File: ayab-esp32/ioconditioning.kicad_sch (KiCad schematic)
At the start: 45 parts, among them J701 CTRL_3v3, J702 CTRL_5V, U701 SN74LVC4245, U702 LM393, U703 LM393

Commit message: Bypass KH910 K-L comparators and add pull-ups
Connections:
- net EOL_R_K: no longer names the net of J702.6 (Pin_6), R711.1, R712.2, R717.1, U701.8 (A6), U703.1
- net EOL_R_L: no longer names the net of J702.7 (Pin_7), R713.1, R714.2, R718.2, U701.9 (A7), U703.7
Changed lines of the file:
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@@
   (wire (pts (xy 102.87 80.01) (xy 102.87 86.36))
     (stroke (width 0) (type default))
-  )
-  (wire (pts (xy 179.07 144.78) (xy 182.88 144.78))
+  )  (wire (pts (xy 107.95 88.9) (xy 107.95 106.68))
     (stroke (width 0) (type default))
-  )
-  (wire (pts (xy 107.95 88.9) (xy 107.95 106.68))
-    (stroke (width 0) (type default))
-  )
-  (wire (pts (xy 182.88 120.65) (xy 181.61 120.65))
-    (stroke (width 0) (type default))
-  )
-  (wire (pts (xy 170.18 99.06) (xy 181.61 99.06))
+  )  (wire (pts (xy 170.18 99.06) (xy 181.61 99.06))
     (stroke (width 0) (type default))
   )
@@
     (effects (font (size 1.27 1.27)) (justify right))
   )
-  (hierarchical_label "EOL_R_L" (shape input) (at 182.88 144.78 0) (fields_autoplaced)
+    (hierarchical_label "EOL_R_N" (shape output) (at 34.29 101.6 180) (fields_autoplaced)
+    (effects (font (size 1.27 1.27)) (justify right))
+  )
+    (hierarchical_label "EOL_R" (shape input) (at 266.7 114.3 0) (fields_autoplaced)
     (effects (font (size 1.27 1.27)) (justify left))
   )
-  (hierarchical_label "EOL_R_N" (shape output) (at 34.29 101.6 180) (fields_autoplaced)
-    (effects (font (size 1.27 1.27)) (justify right))
-  )
-  (hierarchical_label "EOL_R_K" (shape input) (at 182.88 120.65 0) (fields_autoplaced)
-    (effects (font (size 1.27 1.27)) (justify left))
-  )
-  (hierarchical_label "EOL_R" (shape input) (at 266.7 114.3 0) (fields_autoplaced)
-    (effects (font (size 1.27 1.27)) (justify left))
-  )

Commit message: Add passive analog Hall ADC paths
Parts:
- added R735, R736, R737, R738: 10k, Resistor_SMD:R_0603_1608Metric, symbol ayab-lib:R_Small_US
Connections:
- net EOL_L: now also R735.1
- net EOL_R: now also R737.1
- net GND: now also R736.2, R738.2
- net EOL_L_N: no longer names the net of J701.5 (Pin_5), U701.17 (B5)
- net EOL_L_P: no longer names the net of J701.4 (Pin_4), U701.18 (B4)
- net EOL_R_N: no longer names the net of J701.7 (Pin_7), U701.15 (B7)
- net EOL_R_P: no longer names the net of J701.6 (Pin_6), U701.16 (B6)
- new net HALL_L_ADC: R735.2, R736.1
- new net HALL_R_ADC: R737.2, R738.1

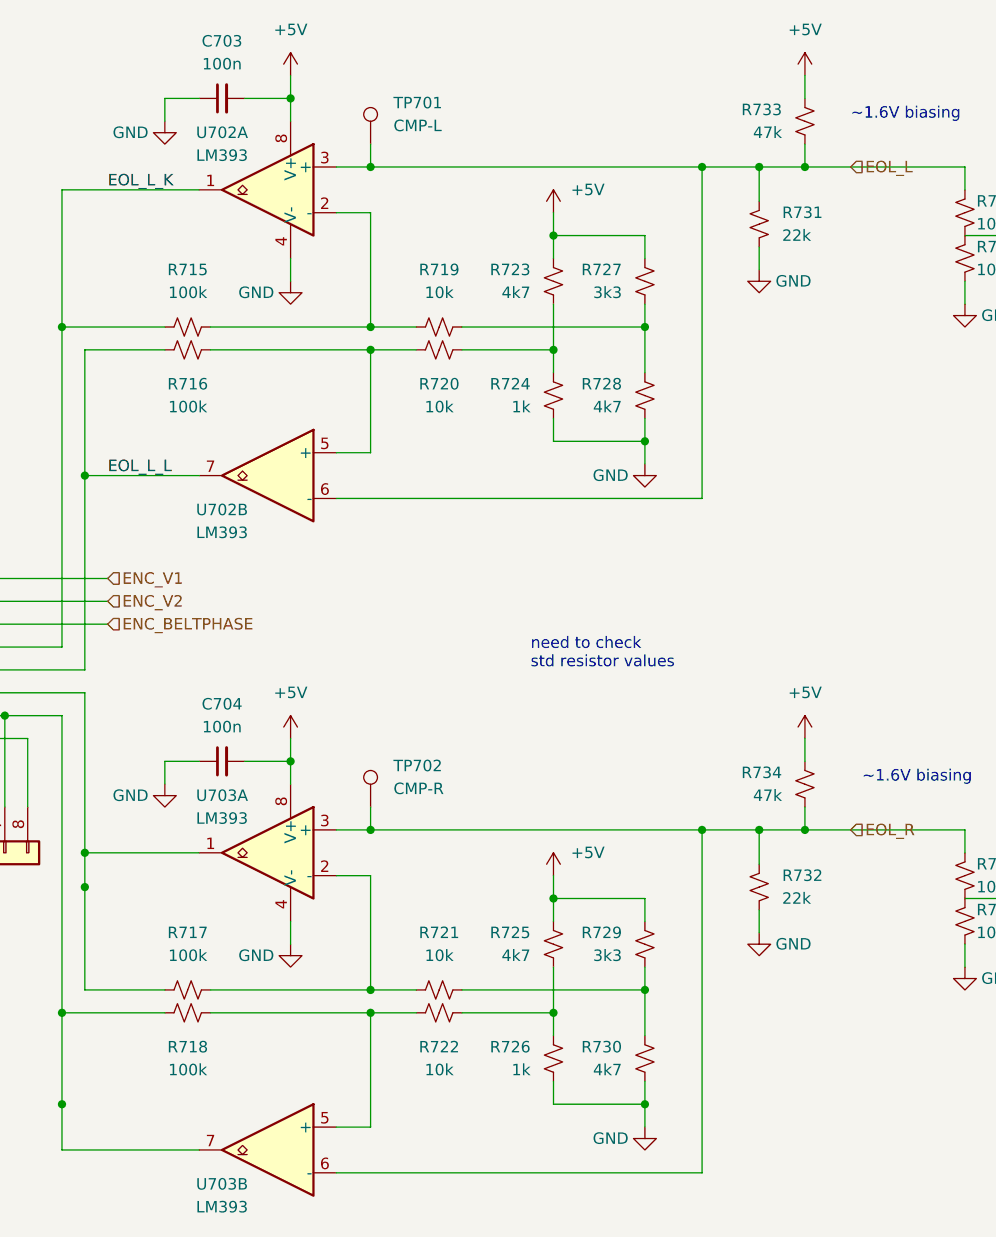
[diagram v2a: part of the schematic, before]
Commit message: Remove obsolete LM393 Hall comparators [skip ci]
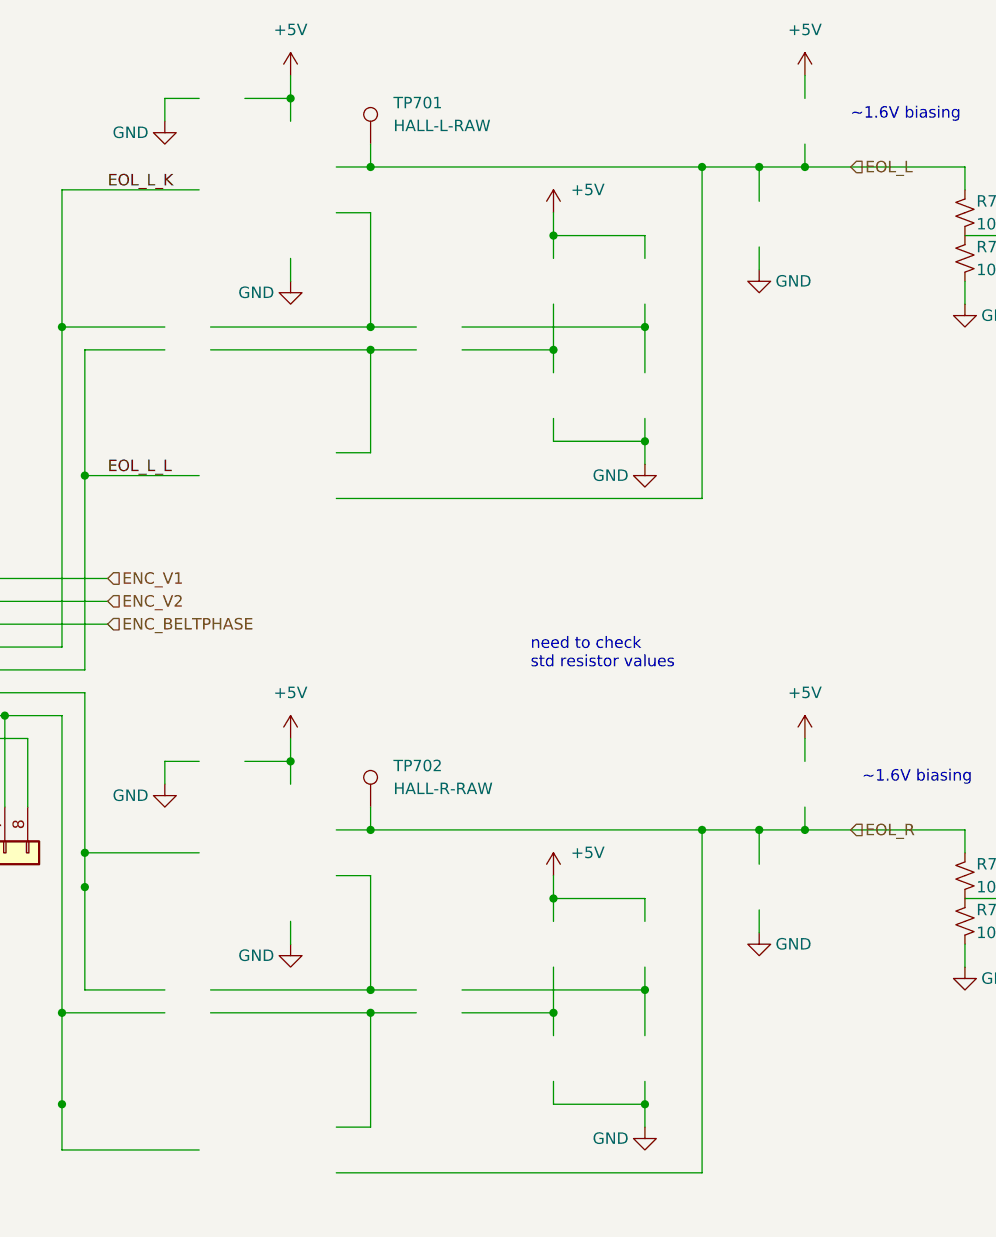
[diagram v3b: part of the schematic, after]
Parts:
- removed C703, C704: 100n, Capacitor_SMD:C_0603_1608Metric, symbol ayab-lib:C_Small
- removed R715, R716, R717, R718: 100k, Resistor_SMD:R_0603_1608Metric, symbol ayab-lib:R_Small_US
- removed R719, R720, R721, R722: 10k, Resistor_SMD:R_0603_1608Metric, symbol ayab-lib:R_Small_US
- removed R723, R725, R728, R730: 4k7, Resistor_SMD:R_0603_1608Metric, symbol ayab-lib:R_Small_US
- removed R724, R726: 1k, Resistor_SMD:R_0603_1608Metric, symbol ayab-lib:R_Small_US
- removed R727, R729: 3k3, Resistor_SMD:R_0603_1608Metric, symbol ayab-lib:R_Small_US
- removed R731, R732: 22k, Resistor_SMD:R_0603_1608Metric, symbol ayab-lib:R_Small_US
- removed R733, R734: 47k, Resistor_SMD:R_0603_1608Metric, symbol ayab-lib:R_Small_US
- removed U702, U703: LM393, Package_SO:SOIC-8_3.9x4.9mm_P1.27mm, symbol ayab-lib:LM393
- TP701: value CMP-L -> HALL-L-RAW
- TP702: value CMP-R -> HALL-R-RAW
